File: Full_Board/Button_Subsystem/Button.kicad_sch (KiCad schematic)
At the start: 6 parts

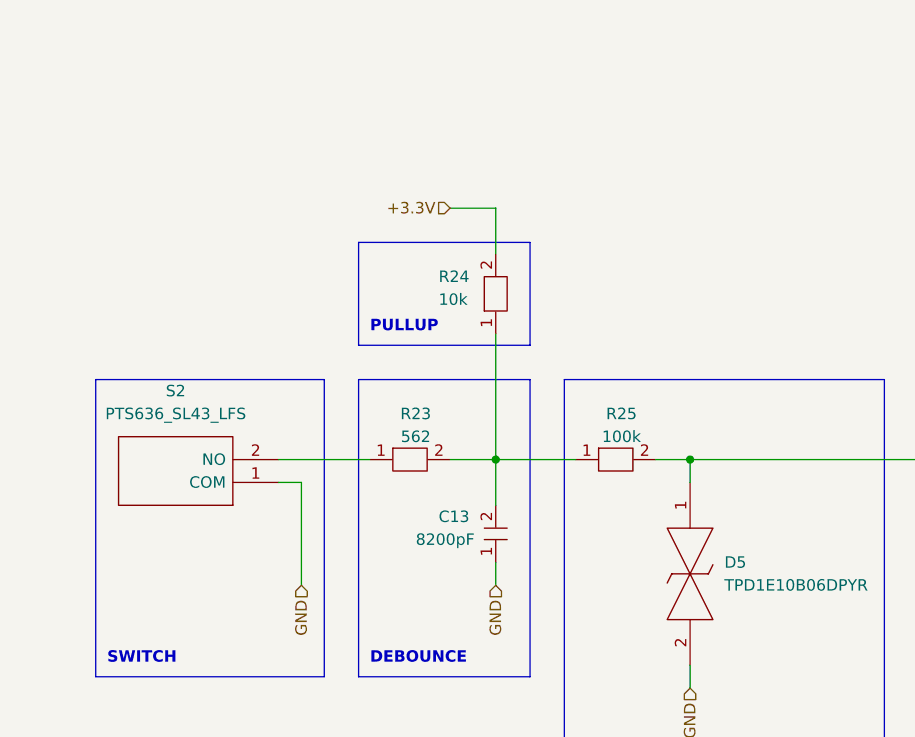
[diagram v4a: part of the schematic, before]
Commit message: Redo sensor network, redo MSP432 connections, redo LED subsystem, add shunts throughout, ERC still passes
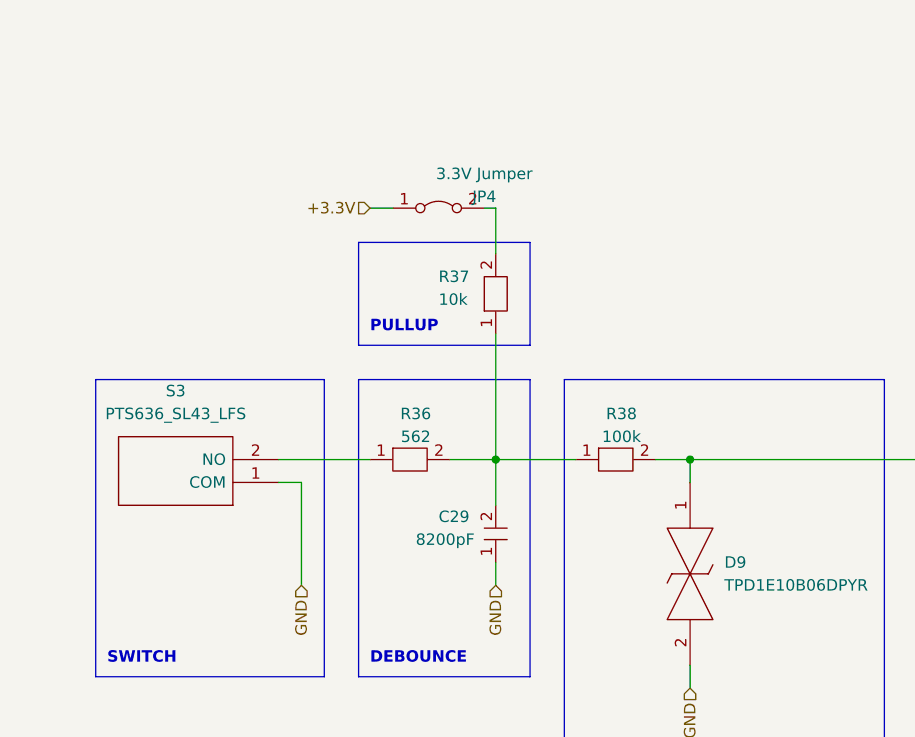
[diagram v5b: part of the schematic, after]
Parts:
- added JP4: 3.3V Jumper, TestPoint:TestPoint_2Pads_Pitch2.54mm_Drill0.8mm, symbol Jumper:Jumper_2_Bridged
- renumbered C13 to C29, D5 to D9, R23 to R36, R24 to R37, R25 to R38, S2 to S3
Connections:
- net +3.3V: now also JP4.1 (A); no longer R37.2
- new net: JP4.2 (B), R37.2
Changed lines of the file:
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@@
     (stroke (width 0) (type default) (color 0 0 0 0))
   )
-  (wire (pts (xy 132.08 66.04) (xy 137.16 66.04))
+  (wire (pts (xy 123.19 66.04) (xy 125.73 66.04))
     (stroke (width 0) (type default) (color 0 0 0 0))
   )
   (polyline (pts (xy 144.78 85.09) (xy 180.34 85.09))
+    (stroke (width 0) (type default) (color 0 0 0 0))
+  )
+  (wire (pts (xy 135.89 66.04) (xy 137.16 66.04))
     (stroke (width 0) (type default) (color 0 0 0 0))
   )
@@
     (effects (font (size 1.27 1.27)) (justify left))
   )
-  (hierarchical_label "+3.3V" (shape input) (at 132.08 66.04 180)
-    (effects (font (size 1.27 1.27)) (justify right))
-  )
-  (symbol (lib_id "RMCF1206FT10K0:10k") (at 137.16 80.01 90)
-    (in_bom yes) (on_board yes)
-    (property "Reference" "R24" (id 0) (at 130.81 73.66 90)
+  (hierarchical_label "+3.3V" (shape input) (at 123.19 66.04 180)
+    (effects (font (size 1.27 1.27)) (justify right))
+  )
+  (symbol (lib_id "RMCF1206FT10K0:10k") (at 137.16 80.01 90) (unit 1)
+    (in_bom yes) (on_board yes)
+    (property "Reference" "R37" (id 0) (at 130.81 73.66 90)
       (effects (font (size 1.27 1.27)) (justify right))
     )
@@
     (pin "2")
   )
-  (symbol (lib_id "C1210C822K2RACAUTO:C1210C822K2RACAUTO") (at 137.16 105.41 90)
-    (in_bom yes) (on_board yes)
-    (property "Reference" "C13" (id 0) (at 130.81 100.33 90)
+  (symbol (lib_id "C1210C822K2RACAUTO:C1210C822K2RACAUTO") (at 137.16 105.41 90) (unit 1)
+    (in_bom yes) (on_board yes)
+    (property "Reference" "C29" (id 0) (at 130.81 100.33 90)
       (effects (font (size 1.27 1.27)) (justify right))
     )
@@
     (pin "2")
   )
-  (symbol (lib_id "CR0402-FX-5620GLF:CR0402-FX-5620GLF") (at 123.19 93.98 0)
-    (in_bom yes) (on_board yes)
-    (property "Reference" "R23" (id 0) (at 128.27 88.9 0))
+  (symbol (lib_id "Jumper:Jumper_2_Bridged") (at 130.81 66.04 0) (unit 1)
+    (in_bom yes) (on_board yes)
+    (property "Reference" "JP4" (id 0) (at 135.89 64.77 0))
+    (property "Value" "3.3V Jumper" (id 1) (at 135.89 62.23 0))
+    (property "Footprint" "TestPoint:TestPoint_2Pads_Pitch2.54mm_Drill0.8mm" (id 2) (at 130.81 66.04 0)
+      (effects (font (size 1.27 1.27)) hide)
+    )
+    (property "Datasheet" "~" (id 3) (at 130.81 66.04 0)
+      (effects (font (size 1.27 1.27)) hide)
+    )
+    (property "Manufacturers Part Number" "PH1-02-UA" (id 4) (at 130.81 66.04 0)
+      (effects (font (size 1.27 1.27)) hide)
+    )
+    (property "Digikey Part Number" "2057-PH1-02-UA-ND" (id 5) (at 130.81 66.04 0)
+      (effects (font (size 1.27 1.27)) hide)
+    )
+    (property "Mouser Part Number" "" (id 6) (at 130.81 66.04 0)
+      (effects (font (size 1.27 1.27)) hide)
+    )
+    (property "Digikey Link" "https://www.digikey.com/en/products/detail/adam-tech/PH1-02-UA/9830266" (id 7) (at 130.81 66.04 0)
+      (effects (font (size 1.27 1.27)) hide)
+    )
+    (property "Mouser Link" "" (id 8) (at 130.81 66.04 0)
+      (effects (font (size 1.27 1.27)) hide)
+    )
+    (pin "1")
+    (pin "2")
+  )
+  (symbol (lib_id "CR0402-FX-5620GLF:CR0402-FX-5620GLF") (at 123.19 93.98 0) (unit 1)
+    (in_bom yes) (on_board yes)
+    (property "Reference" "R36" (id 0) (at 128.27 88.9 0))
     (property "Value" "562" (id 1) (at 128.27 91.44 0))
     (property "Footprint" "CR0402-FX-5620GLF:RESC1005X40N" (id 2) (at 137.16 92.71 0)
@@
     (pin "2")
   )
-  (symbol (lib_id "RCV2512100KFKEGAT:RCV2512100KFKEGAT") (at 146.05 93.98 0)
-    (in_bom yes) (on_board yes)
-    (property "Reference" "R25" (id 0) (at 151.13 88.9 0))
+  (symbol (lib_id "RCV2512100KFKEGAT:RCV2512100KFKEGAT") (at 146.05 93.98 0) (unit 1)
+    (in_bom yes) (on_board yes)
+    (property "Reference" "R38" (id 0) (at 151.13 88.9 0))
     (property "Value" "100k" (id 1) (at 151.13 91.44 0))
     (property "Footprint" "RCV2512100KFKEGAT:RESC6332X70N" (id 2) (at 160.02 92.71 0)
@@
     (pin "2")
   )
-  (symbol (lib_id "PTS636_SL43_LFS:PTS636_SL43_LFS") (at 113.03 96.52 180)
+  (symbol (lib_id "PTS636_SL43_LFS:PTS636_SL43_LFS") (at 113.03 96.52 180) (unit 1)
     (in_bom yes) (on_board yes) (fields_autoplaced)
-    (property "Reference" "S2" (id 0) (at 101.6 86.36 0))
+    (property "Reference" "S3" (id 0) (at 101.6 86.36 0))
     (property "Value" "PTS636_SL43_LFS" (id 1) (at 101.6 88.9 0))
     (property "Footprint" "PTS636_SL43_LFS:PTS636SL43LFS" (id 2) (at 93.98 99.06 0)
@@
     (pin "2")
   )
-  (symbol (lib_id "TPD1E10B06DPYR:TPD1E10B06DPYR") (at 158.75 96.52 270)
-    (in_bom yes) (on_board yes)
-    (property "Reference" "D5" (id 0) (at 162.56 105.41 90)
+  (symbol (lib_id "TPD1E10B06DPYR:TPD1E10B06DPYR") (at 158.75 96.52 270) (unit 1)
+    (in_bom yes) (on_board yes)
+    (property "Reference" "D9" (id 0) (at 162.56 105.41 90)
       (effects (font (size 1.27 1.27)) (justify left))
     )

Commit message: Added LEDs to the power supply
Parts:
- renumbered JP4 to JP10
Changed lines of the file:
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@@
   (symbol (lib_id "Jumper:Jumper_2_Bridged") (at 130.81 66.04 0) (unit 1)
     (in_bom yes) (on_board yes)
-    (property "Reference" "JP4" (id 0) (at 135.89 64.77 0))
+    (property "Reference" "JP10" (id 0) (at 135.89 64.77 0))
     (property "Value" "3.3V Jumper" (id 1) (at 135.89 62.23 0))
     (property "Footprint" "TestPoint:TestPoint_2Pads_Pitch2.54mm_Drill0.8mm" (id 2) (at 130.81 66.04 0)

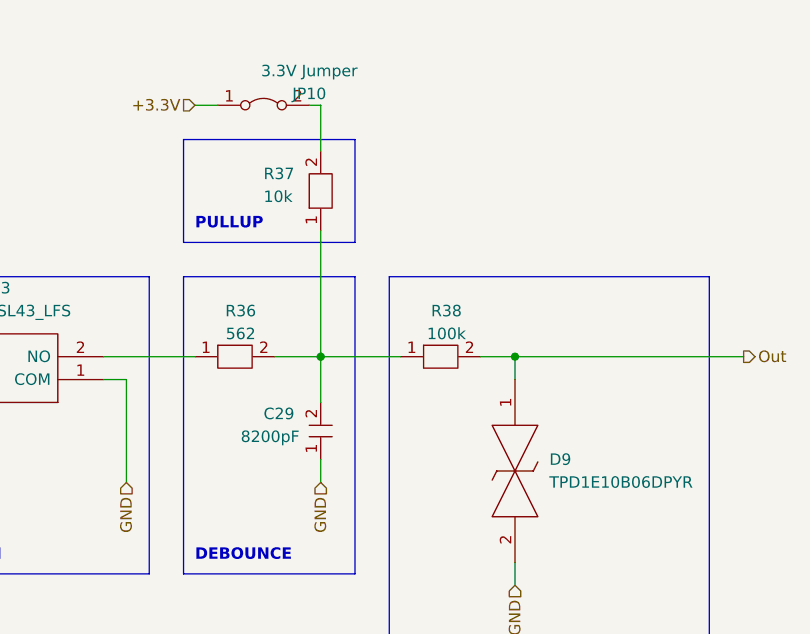
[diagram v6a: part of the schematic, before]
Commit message: Resolve misconfigured components, replace PCB from now completed schematic
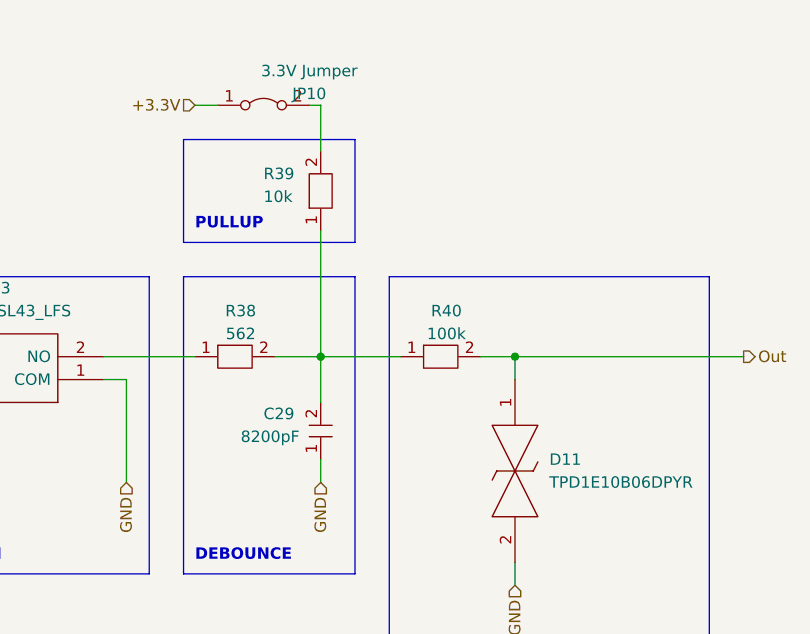
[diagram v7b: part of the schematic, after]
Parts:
- R39: renamed from R37; footprint RESC3225X74N -> RMCF1206FT10K0:RMCF1206FT10K0; Digikey link https://www.digikey.com/en/products/detail/stackpole-electronics-inc/RMCF1206FT10K0/1759669?s=N4IgTCBcDaIEoFkDCAxAjGADANhQFTUwGlMQBdAXyA -> https://www.digikey.com/en/products/detail/stackpole-electronics-inc/RMCF1206FT10K0/1759669
- renumbered D9 to D11, R36 to R38, R38 to R40
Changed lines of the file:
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@@
   (symbol (lib_id "RMCF1206FT10K0:10k") (at 137.16 80.01 90) (unit 1)
     (in_bom yes) (on_board yes)
-    (property "Reference" "R37" (id 0) (at 130.81 73.66 90)
+    (property "Reference" "R39" (id 0) (at 130.81 73.66 90)
       (effects (font (size 1.27 1.27)) (justify right))
     )
@@
       (effects (font (size 1.27 1.27)) (justify right))
     )
-    (property "Footprint" "RESC3225X74N" (id 2) (at 135.89 66.04 0)
+    (property "Footprint" "RMCF1206FT10K0:RMCF1206FT10K0" (id 2) (at 135.89 66.04 0)
       (effects (font (size 1.27 1.27)) (justify left) hide)
     )
-    (property "Datasheet" "https://www.vishay.com/docs/68043/crma.pdf" (id 3) (at 138.43 66.04 0)
+    (property "Datasheet" "https://www.seielect.com/catalog/sei-rmcf_rmcp.pdf" (id 3) (at 138.43 66.04 0)
       (effects (font (size 1.27 1.27)) (justify left) hide)
     )
@@
       (effects (font (size 1.27 1.27)) (justify left) hide)
     )
-    (property "Digikey link" "https://www.digikey.com/en/products/detail/stackpole-electronics-inc/RMCF1206FT10K0/1759669?s=N4IgTCBcDaIEoFkDCAxAjGADANhQFTUwGlMQBdAXyA" (id 7) (at 148.59 66.04 0)
+    (property "Digikey link" "https://www.digikey.com/en/products/detail/stackpole-electronics-inc/RMCF1206FT10K0/1759669" (id 7) (at 148.59 66.04 0)
       (effects (font (size 1.27 1.27)) (justify left) hide)
     )
@@
   (symbol (lib_id "CR0402-FX-5620GLF:CR0402-FX-5620GLF") (at 123.19 93.98 0) (unit 1)
     (in_bom yes) (on_board yes)
-    (property "Reference" "R36" (id 0) (at 128.27 88.9 0))
+    (property "Reference" "R38" (id 0) (at 128.27 88.9 0))
     (property "Value" "562" (id 1) (at 128.27 91.44 0))
     (property "Footprint" "CR0402-FX-5620GLF:RESC1005X40N" (id 2) (at 137.16 92.71 0)
@@
   (symbol (lib_id "RCV2512100KFKEGAT:RCV2512100KFKEGAT") (at 146.05 93.98 0) (unit 1)
     (in_bom yes) (on_board yes)
-    (property "Reference" "R38" (id 0) (at 151.13 88.9 0))
+    (property "Reference" "R40" (id 0) (at 151.13 88.9 0))
     (property "Value" "100k" (id 1) (at 151.13 91.44 0))
     (property "Footprint" "RCV2512100KFKEGAT:RESC6332X70N" (id 2) (at 160.02 92.71 0)
@@
   (symbol (lib_id "TPD1E10B06DPYR:TPD1E10B06DPYR") (at 158.75 96.52 270) (unit 1)
     (in_bom yes) (on_board yes)
-    (property "Reference" "D9" (id 0) (at 162.56 105.41 90)
+    (property "Reference" "D11" (id 0) (at 162.56 105.41 90)
       (effects (font (size 1.27 1.27)) (justify left))
     )

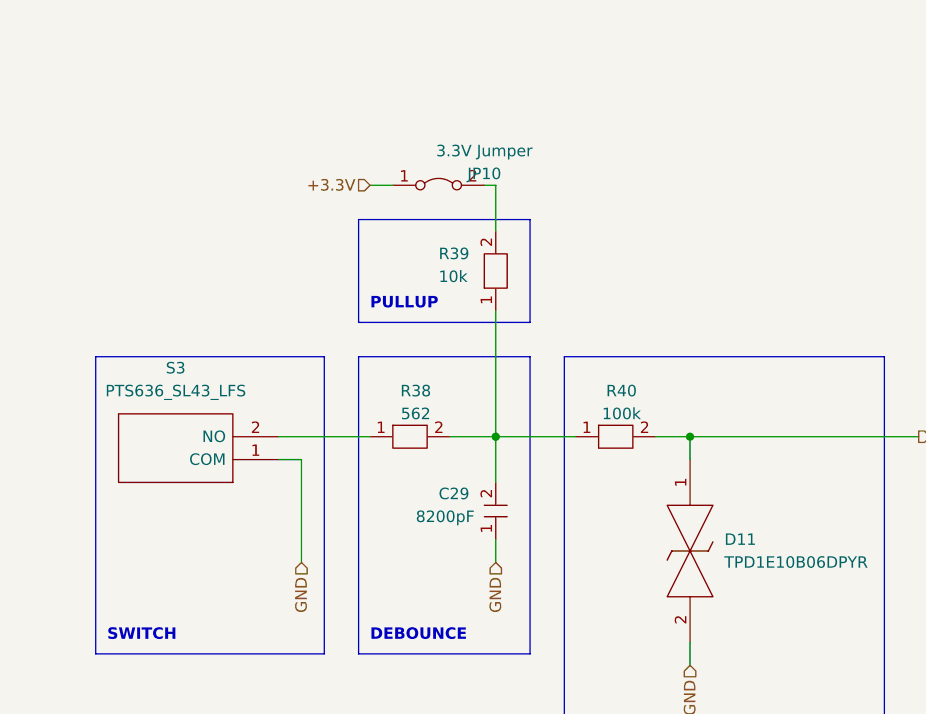
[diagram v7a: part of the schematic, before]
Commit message: Added USB connector for the pi
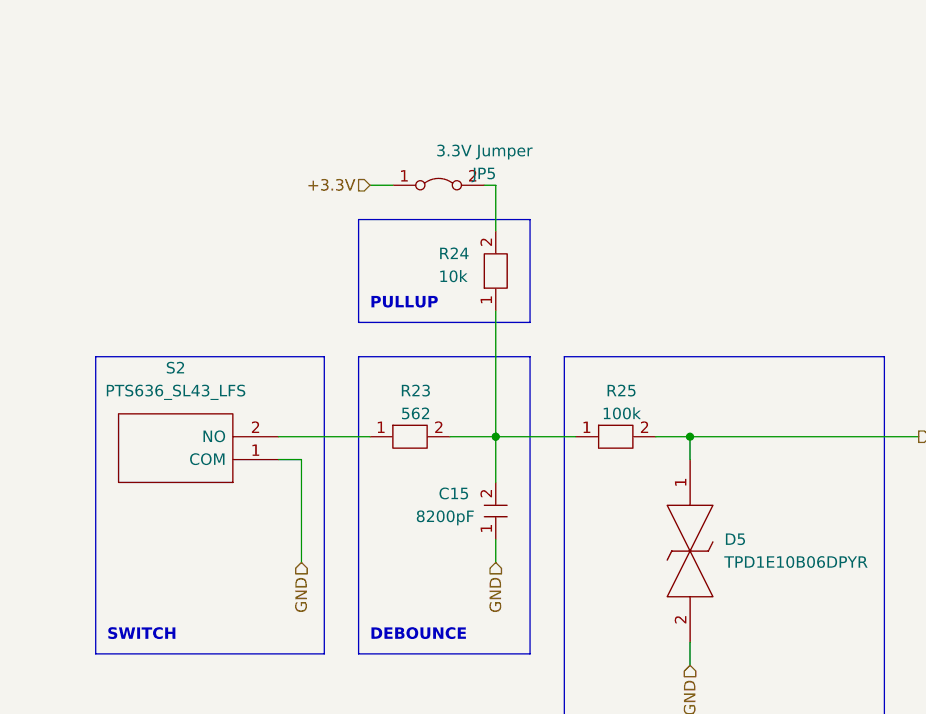
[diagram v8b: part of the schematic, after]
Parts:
- renumbered C29 to C15, D11 to D5, JP10 to JP5, R38 to R23, R39 to R24, R40 to R25, S3 to S2
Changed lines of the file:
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@@
     (effects (font (size 1.27 1.27)) (justify right))
   )
-  (symbol (lib_id "RMCF1206FT10K0:10k") (at 137.16 80.01 90) (unit 1)
+  (symbol (lib_id "RMCF1206FT10K0:10k") (at 137.16 80.01 90)
     (in_bom yes) (on_board yes)
-    (property "Reference" "R39" (id 0) (at 130.81 73.66 90)
+    (property "Reference" "R24" (id 0) (at 130.81 73.66 90)
       (effects (font (size 1.27 1.27)) (justify right))
     )
@@
     (pin "2")
   )
-  (symbol (lib_id "C1210C822K2RACAUTO:C1210C822K2RACAUTO") (at 137.16 105.41 90) (unit 1)
+  (symbol (lib_id "C1210C822K2RACAUTO:C1210C822K2RACAUTO") (at 137.16 105.41 90)
     (in_bom yes) (on_board yes)
-    (property "Reference" "C29" (id 0) (at 130.81 100.33 90)
+    (property "Reference" "C15" (id 0) (at 130.81 100.33 90)
       (effects (font (size 1.27 1.27)) (justify right))
     )
@@
     (pin "2")
   )
-  (symbol (lib_id "Jumper:Jumper_2_Bridged") (at 130.81 66.04 0) (unit 1)
+  (symbol (lib_id "Jumper:Jumper_2_Bridged") (at 130.81 66.04 0)
     (in_bom yes) (on_board yes)
-    (property "Reference" "JP10" (id 0) (at 135.89 64.77 0))
+    (property "Reference" "JP5" (id 0) (at 135.89 64.77 0))
     (property "Value" "3.3V Jumper" (id 1) (at 135.89 62.23 0))
     (property "Footprint" "TestPoint:TestPoint_2Pads_Pitch2.54mm_Drill0.8mm" (id 2) (at 130.81 66.04 0)
@@
     (pin "2")
   )
-  (symbol (lib_id "CR0402-FX-5620GLF:CR0402-FX-5620GLF") (at 123.19 93.98 0) (unit 1)
+  (symbol (lib_id "CR0402-FX-5620GLF:CR0402-FX-5620GLF") (at 123.19 93.98 0)
     (in_bom yes) (on_board yes)
-    (property "Reference" "R38" (id 0) (at 128.27 88.9 0))
+    (property "Reference" "R23" (id 0) (at 128.27 88.9 0))
     (property "Value" "562" (id 1) (at 128.27 91.44 0))
     (property "Footprint" "CR0402-FX-5620GLF:RESC1005X40N" (id 2) (at 137.16 92.71 0)
@@
     (pin "2")
   )
-  (symbol (lib_id "RCV2512100KFKEGAT:RCV2512100KFKEGAT") (at 146.05 93.98 0) (unit 1)
+  (symbol (lib_id "RCV2512100KFKEGAT:RCV2512100KFKEGAT") (at 146.05 93.98 0)
     (in_bom yes) (on_board yes)
-    (property "Reference" "R40" (id 0) (at 151.13 88.9 0))
+    (property "Reference" "R25" (id 0) (at 151.13 88.9 0))
     (property "Value" "100k" (id 1) (at 151.13 91.44 0))
     (property "Footprint" "RCV2512100KFKEGAT:RESC6332X70N" (id 2) (at 160.02 92.71 0)
@@
     (pin "2")
   )
-  (symbol (lib_id "PTS636_SL43_LFS:PTS636_SL43_LFS") (at 113.03 96.52 180) (unit 1)
+  (symbol (lib_id "PTS636_SL43_LFS:PTS636_SL43_LFS") (at 113.03 96.52 180)
     (in_bom yes) (on_board yes) (fields_autoplaced)
-    (property "Reference" "S3" (id 0) (at 101.6 86.36 0))
+    (property "Reference" "S2" (id 0) (at 101.6 86.36 0))
     (property "Value" "PTS636_SL43_LFS" (id 1) (at 101.6 88.9 0))
     (property "Footprint" "PTS636_SL43_LFS:PTS636SL43LFS" (id 2) (at 93.98 99.06 0)
@@
     (pin "2")
   )
-  (symbol (lib_id "TPD1E10B06DPYR:TPD1E10B06DPYR") (at 158.75 96.52 270) (unit 1)
+  (symbol (lib_id "TPD1E10B06DPYR:TPD1E10B06DPYR") (at 158.75 96.52 270)
     (in_bom yes) (on_board yes)
-    (property "Reference" "D11" (id 0) (at 162.56 105.41 90)
+    (property "Reference" "D5" (id 0) (at 162.56 105.41 90)
       (effects (font (size 1.27 1.27)) (justify left))
     )
